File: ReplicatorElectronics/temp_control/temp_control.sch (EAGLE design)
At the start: 10 parts, among them J1 SBH11-PBPC-D05-ST-BK, J2 OSTVN04A150, Q1 IRL540N, T1 MMBT2222A, T2 MMBT2222A, T3 MMBT3906LT1

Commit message: 6/3/12: Added LED.
~ 0.5 hr.
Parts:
- added LED1: RED, resistor:R-US_R0603
- added R3: 3.9k, resistor:R-US_R0603
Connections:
- new net N$1: LED1.2, R3.1
- net GND: now also LED1.1
- net N$6: now also R3.2
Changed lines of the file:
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@@
 <part name="D1" library="chipKIT_Max32" deviceset="DISCRETE_DIODE" device="SMA" value="B340A-13-F"/>
 <part name="J1" library="SBH11-PBPC-D05-ST-BK" deviceset="SBH11-PBPC-D05-ST-BK" device=""/>
+<part name="R3" library="resistor" deviceset="R-US_" device="R0603" value="3.9k"/>
+<part name="LED1" library="resistor" deviceset="R-US_" device="R0603" value="RED"/>
+<part name="GND3" library="supply1" deviceset="GND" device=""/>
 </parts>
 <sheets>
@@
 <instance part="D1" gate="G$1" x="66.04" y="60.96" rot="R270"/>
 <instance part="J1" gate="G$1" x="22.86" y="22.86"/>
+<instance part="R3" gate="G$1" x="12.7" y="63.5" rot="R90"/>
+<instance part="LED1" gate="G$1" x="12.7" y="50.8" rot="R90"/>
+<instance part="GND3" gate="1" x="12.7" y="43.18"/>
 </instances>
 <busses>
@@
 <pinref part="GND2" gate="1" pin="GND"/>
 </segment>
+<segment>
+<pinref part="LED1" gate="G$1" pin="1"/>
+<pinref part="GND3" gate="1" pin="GND"/>
+</segment>
 </net>
 <net name="THERM1" class="0">
@@
 <wire x1="7.62" y1="73.66" x2="2.54" y2="73.66" width="0.1524" layer="91"/>
 <pinref part="Q1" gate="G$1" pin="G"/>
-<wire x1="17.78" y1="71.12" x2="7.62" y2="71.12" width="0.1524" layer="91"/>
+<wire x1="17.78" y1="71.12" x2="12.7" y2="71.12" width="0.1524" layer="91"/>
 <junction x="7.62" y="71.12"/>
+<pinref part="R3" gate="G$1" pin="2"/>
+<wire x1="12.7" y1="71.12" x2="7.62" y2="71.12" width="0.1524" layer="91"/>
+<wire x1="12.7" y1="68.58" x2="12.7" y2="71.12" width="0.1524" layer="91"/>
+<junction x="12.7" y="71.12"/>
 </segment>
 </net>
@@
 </segment>
 </net>
+<net name="N$1" class="0">
+<segment>
+<pinref part="R3" gate="G$1" pin="1"/>
+<wire x1="12.7" y1="58.42" x2="12.7" y2="55.88" width="0.1524" layer="91"/>
+<pinref part="LED1" gate="G$1" pin="2"/>
+</segment>
+</net>

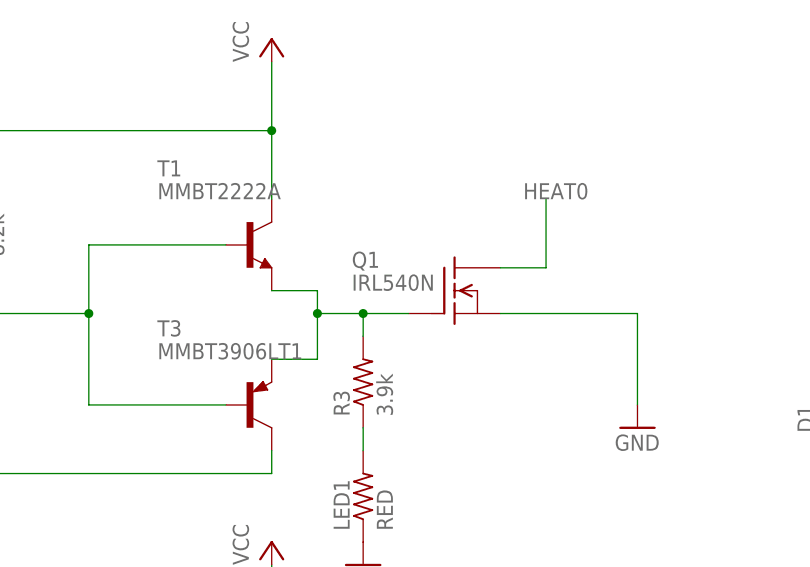
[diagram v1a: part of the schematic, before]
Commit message: 5/10/12: Changed part number for Q1 to one which costs less.
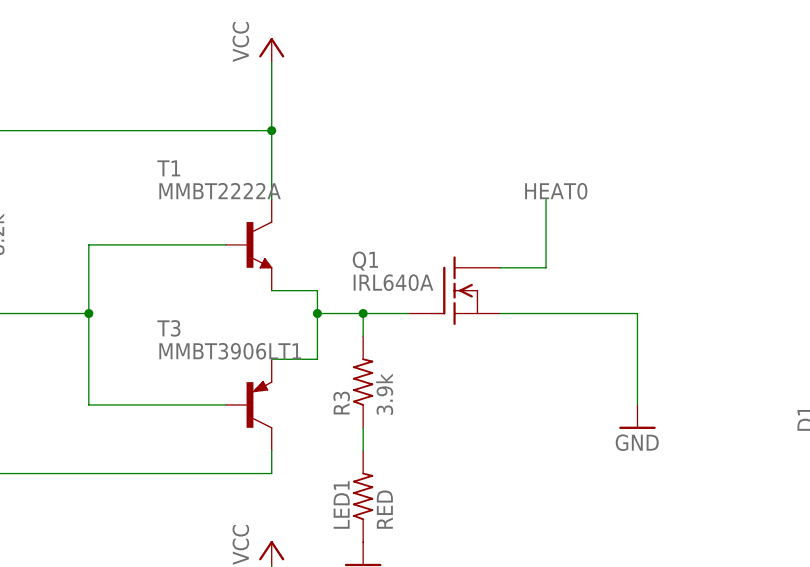
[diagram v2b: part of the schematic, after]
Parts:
- Q1: value IRL540N -> IRL640A
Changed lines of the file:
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@@
 </classes>
 <parts>
-<part name="Q1" library="transistor-fet" deviceset="SUP75N06-08" device="" value="IRL540N"/>
+<part name="Q1" library="transistor-fet" deviceset="SUP75N06-08" device="" value="IRL640A"/>
 <part name="P+1" library="supply1" deviceset="VCC" device=""/>
 <part name="GND1" library="supply1" deviceset="GND" device=""/>

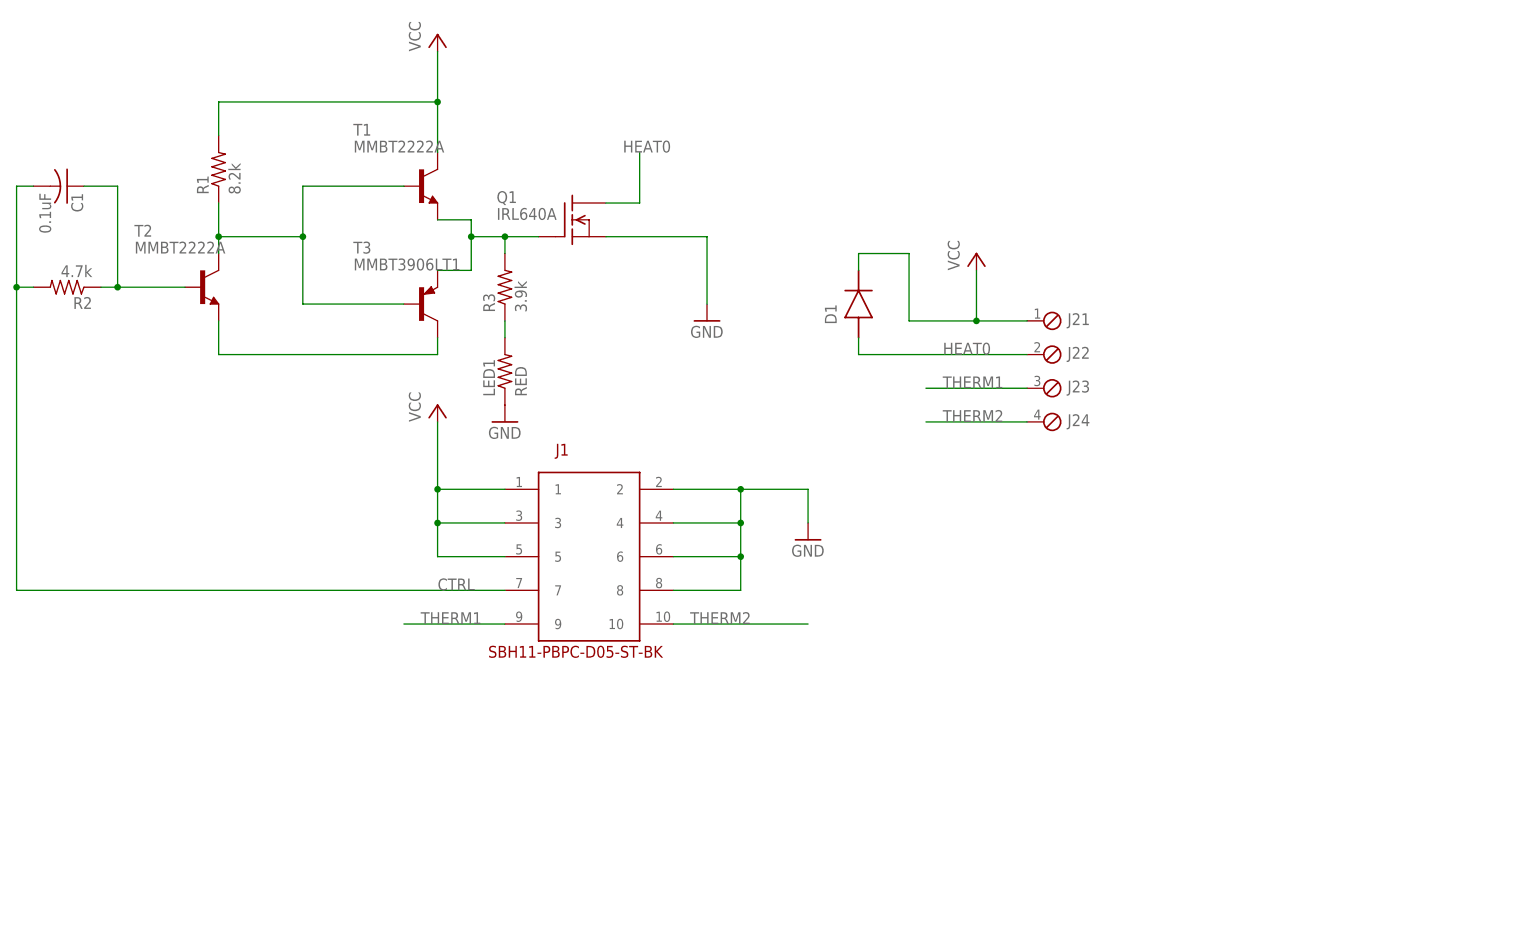
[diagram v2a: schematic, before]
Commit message: 6/12/12: Added linearization circuit for potential thermocouple use. Can be DNP if not used.
~ 2 hrs.
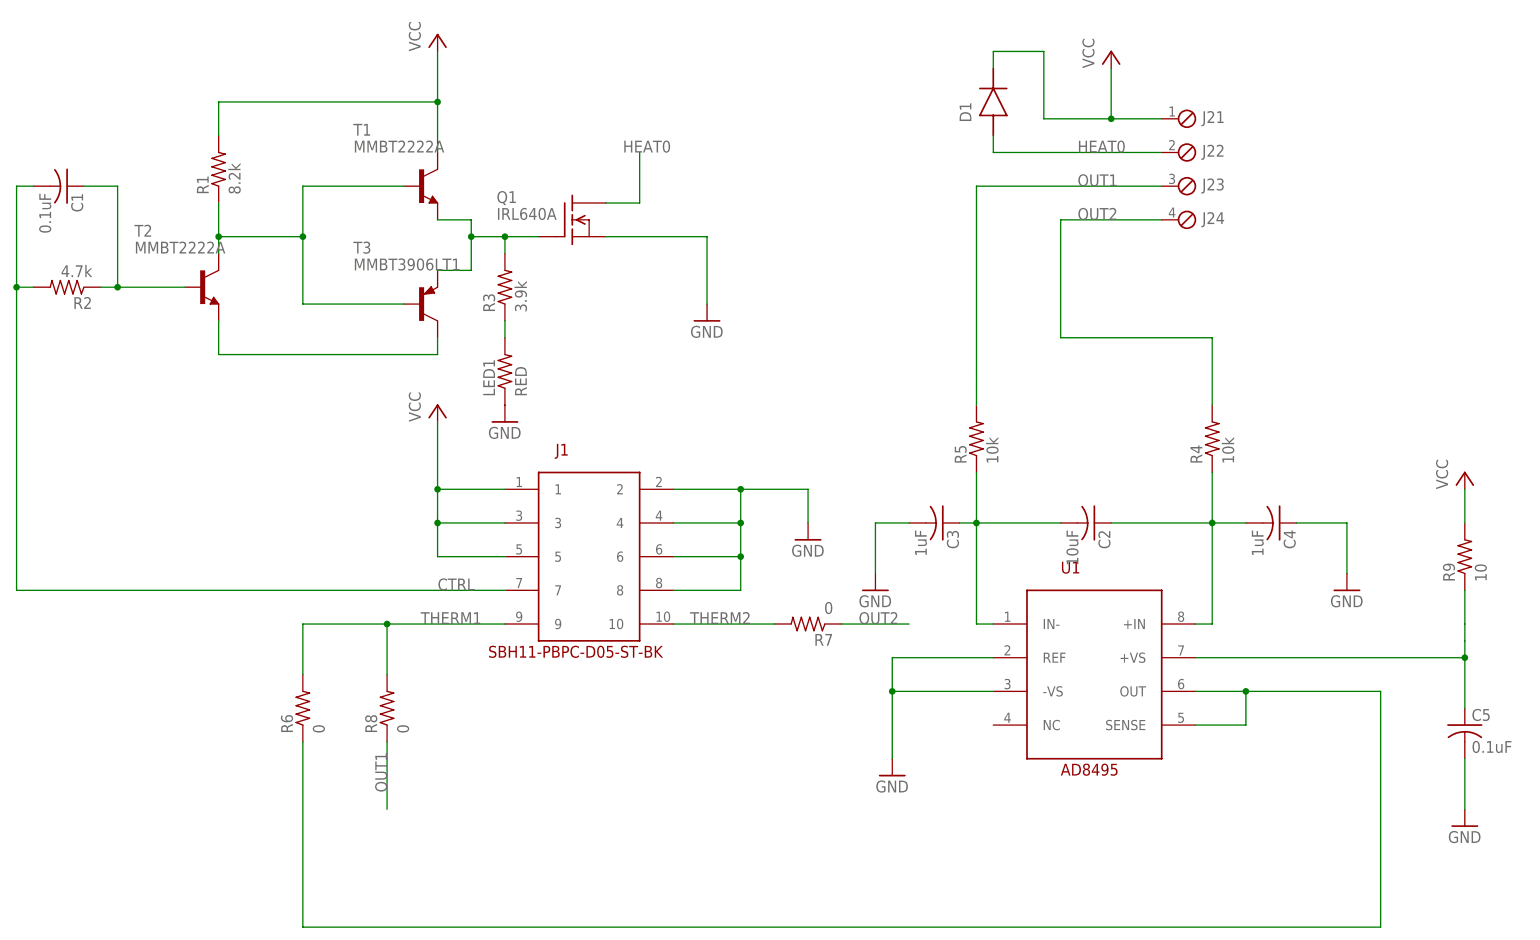
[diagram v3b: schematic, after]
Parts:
- added C2: 10uF, resistor:C-USC0603
- added C3, C4: 1uF, resistor:C-USC0603
- added C5: 0.1uF, resistor:C-USC0603
- added R4, R5: 10k, resistor:R-US_R0603
- added R6, R7, R8: 0, resistor:R-US_R0603
- added R9: 10, resistor:R-US_R0603
- added U1: AD8495, analog-devices:AD8495
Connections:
- new net N$12: R6.1, U1.OUT, U1.SENSE
- new net N$2: C2.2, C3.1, R5.1, U1.IN-
- new net N$5: C2.1, C4.2, R4.1, U1.+IN
- new net N$7: C5.1, R9.1, U1.+VS
- new net OUT1: J23.1, R5.2, R8.1
- new net OUT2: J24.1, R4.2, R7.1
- net GND: now also C3.2, C4.1, C5.2, U1.-VS, U1.REF
- net THERM1: now also R6.2, R8.2; no longer J23.1
- net THERM2: now also R7.2; no longer J24.1
- net VCC: now also R9.2
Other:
- moved on the sheet: D1, J21, J22, J23, J24
